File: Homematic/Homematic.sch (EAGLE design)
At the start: 26 parts, among them IC1 3.3V, IC2 3.3V, P1 DF11-06-2DS, Q1 BS170

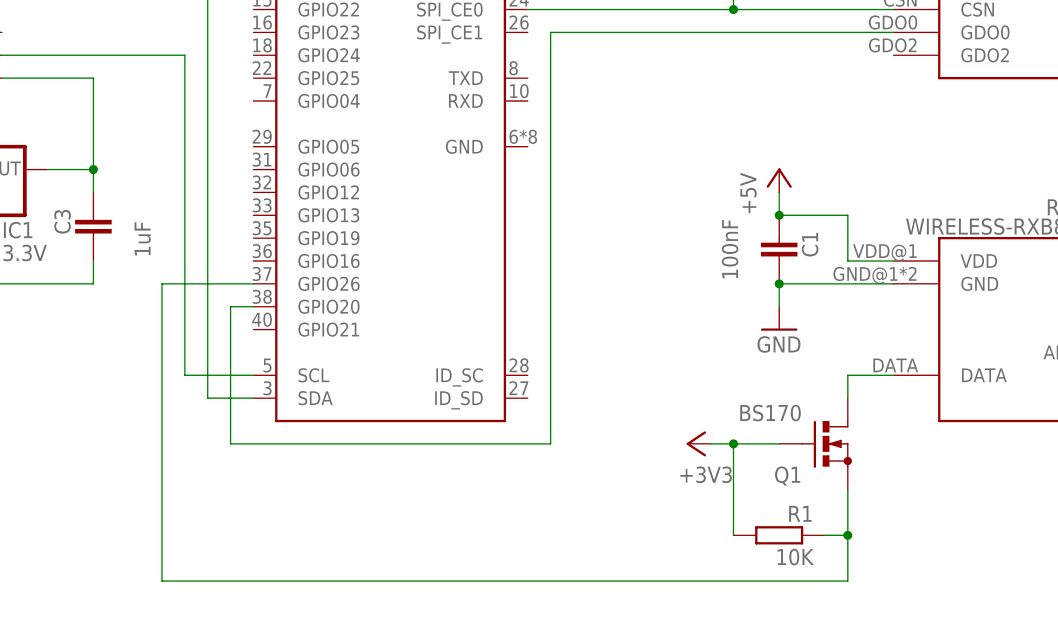
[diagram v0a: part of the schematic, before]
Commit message: Fix RXB8 package. Add low pass filter.
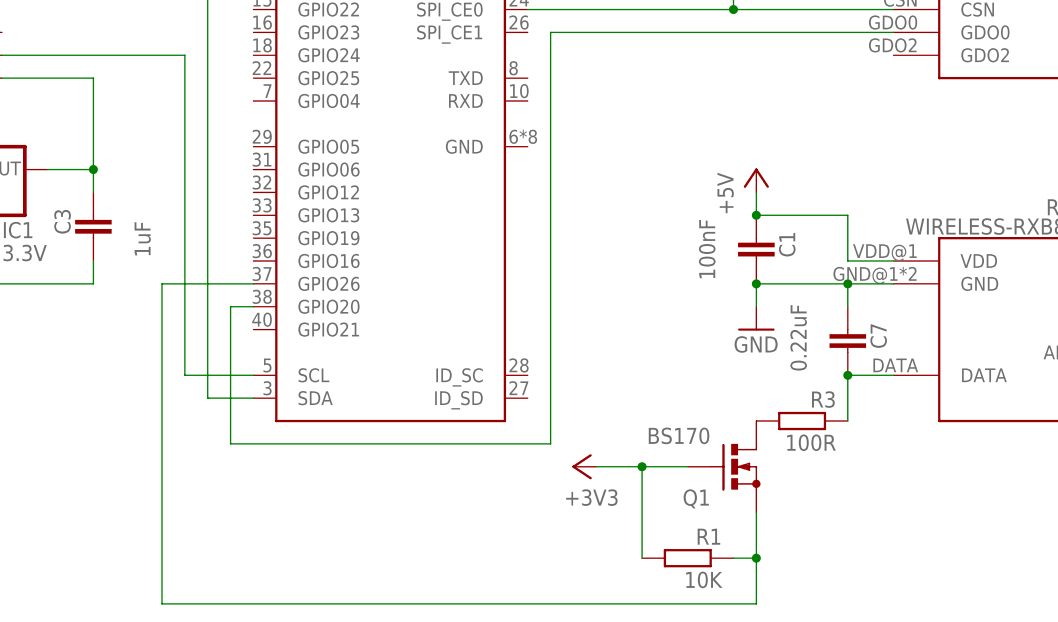
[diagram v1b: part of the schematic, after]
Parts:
- added C7: 0.22uF, capacitor-wima:C2,5-3
- added R3: 100R, rcl:R-EU_0204/5
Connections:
- new net N$11: Q1.D, R3.2
- net GND: now also C7.1
- net N$3: now also C7.2, R3.1; no longer Q1.D
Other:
- moved on the sheet: C1, Q1, R1
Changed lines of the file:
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@@
 <part name="+3V1" library="supply1" deviceset="+3V3" device=""/>
 <part name="+3V2" library="supply1" deviceset="+3V3" device=""/>
+<part name="R3" library="rcl" deviceset="R-EU_" device="0204/5" value="100R">
+<attribute name="MF" value=""/>
+<attribute name="MPN" value=""/>
+<attribute name="OC_FARNELL" value="unknown"/>
+</part>
+<part name="C7" library="capacitor-wima" deviceset="C" device="2,5-3" value="0.22uF"/>
 </parts>
 <sheets>
@@
 </instance>
 <instance part="GND2" gate="1" x="256.54" y="27.94"/>
-<instance part="Q1" gate="1" x="208.28" y="27.94" smashed="yes">
-<attribute name="OC_FARNELL" x="208.28" y="27.94" size="1.778" layer="96" rot="R270" display="off"/>
-<attribute name="MF" x="208.28" y="27.94" size="1.778" layer="96" rot="R270" display="off"/>
-<attribute name="MPN" x="208.28" y="27.94" size="1.778" layer="96" rot="R270" display="off"/>
-<attribute name="NAME" x="205.74" y="25.4" size="1.778" layer="95" align="top-right"/>
-<attribute name="VALUE" x="205.74" y="30.48" size="1.778" layer="96" align="bottom-right"/>
-</instance>
-<instance part="R1" gate="G$1" x="203.2" y="17.78" rot="MR0">
-<attribute name="OC_FARNELL" x="203.2" y="17.78" size="1.778" layer="96" rot="MR270" display="off"/>
-<attribute name="MF" x="203.2" y="17.78" size="1.778" layer="96" rot="MR270" display="off"/>
-<attribute name="MPN" x="203.2" y="17.78" size="1.778" layer="96" rot="MR270" display="off"/>
+<instance part="Q1" gate="1" x="198.12" y="25.4" smashed="yes">
+<attribute name="OC_FARNELL" x="198.12" y="25.4" size="1.778" layer="96" rot="R270" display="off"/>
+<attribute name="MF" x="198.12" y="25.4" size="1.778" layer="96" rot="R270" display="off"/>
+<attribute name="MPN" x="198.12" y="25.4" size="1.778" layer="96" rot="R270" display="off"/>
+<attribute name="NAME" x="195.58" y="22.86" size="1.778" layer="95" align="top-right"/>
+<attribute name="VALUE" x="195.58" y="27.94" size="1.778" layer="96" align="bottom-right"/>
+</instance>
+<instance part="R1" gate="G$1" x="193.04" y="15.24" rot="MR0">
+<attribute name="OC_FARNELL" x="193.04" y="15.24" size="1.778" layer="96" rot="MR270" display="off"/>
+<attribute name="MF" x="193.04" y="15.24" size="1.778" layer="96" rot="MR270" display="off"/>
+<attribute name="MPN" x="193.04" y="15.24" size="1.778" layer="96" rot="MR270" display="off"/>
 </instance>
 <instance part="MP1584-2" gate="G$1" x="50.8" y="93.98"/>
@@
 <attribute name="MPN" x="198.12" y="91.44" size="1.778" layer="96" rot="MR0" display="off"/>
 </instance>
-<instance part="GND6" gate="1" x="203.2" y="40.64"/>
-<instance part="C1" gate="G$1" x="203.2" y="50.8" smashed="yes" rot="MR0">
-<attribute name="NAME" x="205.74" y="48.641" size="1.778" layer="95" rot="MR90"/>
-<attribute name="VALUE" x="196.85" y="46.101" size="1.778" layer="96" rot="MR90"/>
-</instance>
-<instance part="P+4" gate="1" x="203.2" y="58.42"/>
+<instance part="GND6" gate="1" x="200.66" y="40.64"/>
+<instance part="C1" gate="G$1" x="200.66" y="50.8" smashed="yes" rot="MR0">
+<attribute name="NAME" x="203.2" y="48.641" size="1.778" layer="95" rot="MR90"/>
+<attribute name="VALUE" x="194.31" y="46.101" size="1.778" layer="96" rot="MR90"/>
+</instance>
+<instance part="P+4" gate="1" x="200.66" y="58.42"/>
 <instance part="+3V1" gate="G$1" x="213.36" y="129.54"/>
-<instance part="+3V2" gate="G$1" x="193.04" y="27.94" rot="R90"/>
+<instance part="+3V2" gate="G$1" x="180.34" y="25.4" rot="R90"/>
+<instance part="R3" gate="G$1" x="205.74" y="30.48" rot="MR0">
+<attribute name="OC_FARNELL" x="205.74" y="30.48" size="1.778" layer="96" rot="MR270" display="off"/>
+<attribute name="MF" x="205.74" y="30.48" size="1.778" layer="96" rot="MR270" display="off"/>
+<attribute name="MPN" x="205.74" y="30.48" size="1.778" layer="96" rot="MR270" display="off"/>
+</instance>
+<instance part="C7" gate="G$1" x="210.82" y="40.64" smashed="yes" rot="MR0">
+<attribute name="NAME" x="213.36" y="38.481" size="1.778" layer="95" rot="MR90"/>
+<attribute name="VALUE" x="204.47" y="35.941" size="1.778" layer="96" rot="MR90"/>
+</instance>
 </instances>
 <busses>
@@
 <pinref part="RXB8" gate="G$1" pin="GND"/>
 <pinref part="GND6" gate="1" pin="GND"/>
-<wire x1="215.9" y1="45.72" x2="203.2" y2="45.72" width="0.1524" layer="91"/>
-<wire x1="203.2" y1="45.72" x2="203.2" y2="43.18" width="0.1524" layer="91"/>
+<wire x1="215.9" y1="45.72" x2="210.82" y2="45.72" width="0.1524" layer="91"/>
+<wire x1="210.82" y1="45.72" x2="200.66" y2="45.72" width="0.1524" layer="91"/>
+<wire x1="200.66" y1="45.72" x2="200.66" y2="43.18" width="0.1524" layer="91"/>
 <pinref part="C1" gate="G$1" pin="2"/>
-<junction x="203.2" y="45.72"/>
-</segment>
-</net>
-<net name="N$69" class="0">
-<segment>
-<pinref part="Q1" gate="1" pin="S"/>
-<wire x1="210.82" y1="22.86" x2="210.82" y2="17.78" width="0.1524" layer="91"/>
-<wire x1="208.28" y1="17.78" x2="210.82" y2="17.78" width="0.1524" layer="91"/>
-<wire x1="210.82" y1="17.78" x2="210.82" y2="12.7" width="0.1524" layer="91"/>
-<wire x1="210.82" y1="12.7" x2="134.62" y2="12.7" width="0.1524" layer="91"/>
-<wire x1="134.62" y1="12.7" x2="134.62" y2="45.72" width="0.1524" layer="91"/>
-<pinref part="R1" gate="G$1" pin="1"/>
-<junction x="210.82" y="17.78"/>
-<pinref part="RPI" gate="G$1" pin="GPIO26"/>
-<wire x1="134.62" y1="45.72" x2="144.78" y2="45.72" width="0.1524" layer="91"/>
+<junction x="200.66" y="45.72"/>
+<pinref part="C7" gate="G$1" pin="1"/>
+<wire x1="210.82" y1="43.18" x2="210.82" y2="45.72" width="0.1524" layer="91"/>
+<junction x="210.82" y="45.72"/>
 </segment>
 </net>
 <net name="N$3" class="0">
 <segment>
-<pinref part="Q1" gate="1" pin="D"/>
-<wire x1="210.82" y1="35.56" x2="210.82" y2="33.02" width="0.1524" layer="91"/>
 <wire x1="210.82" y1="35.56" x2="215.9" y2="35.56" width="0.1524" layer="91"/>
 <pinref part="RXB8" gate="G$1" pin="DATA"/>
+<pinref part="C7" gate="G$1" pin="2"/>
+<pinref part="R3" gate="G$1" pin="1"/>
+<wire x1="210.82" y1="35.56" x2="210.82" y2="30.48" width="0.1524" layer="91"/>
+<junction x="210.82" y="35.56"/>
 </segment>
 </net>
@@
 <segment>
 <pinref part="C1" gate="G$1" pin="1"/>
-<wire x1="203.2" y1="55.88" x2="203.2" y2="53.34" width="0.1524" layer="91"/>
-<wire x1="203.2" y1="53.34" x2="210.82" y2="53.34" width="0.1524" layer="91"/>
+<wire x1="200.66" y1="55.88" x2="200.66" y2="53.34" width="0.1524" layer="91"/>
+<wire x1="200.66" y1="53.34" x2="210.82" y2="53.34" width="0.1524" layer="91"/>
 <wire x1="210.82" y1="53.34" x2="210.82" y2="48.26" width="0.1524" layer="91"/>
 <pinref part="RXB8" gate="G$1" pin="VDD"/>
 <wire x1="210.82" y1="48.26" x2="215.9" y2="48.26" width="0.1524" layer="91"/>
 <pinref part="P+4" gate="1" pin="+5V"/>
-<junction x="203.2" y="53.34"/>
+<junction x="200.66" y="53.34"/>
 </segment>
 </net>
@@
 <pinref part="R1" gate="G$1" pin="2"/>
 <pinref part="Q1" gate="1" pin="G"/>
-<wire x1="203.2" y1="27.94" x2="198.12" y2="27.94" width="0.1524" layer="91"/>
-<wire x1="198.12" y1="27.94" x2="198.12" y2="17.78" width="0.1524" layer="91"/>
+<wire x1="193.04" y1="25.4" x2="187.96" y2="25.4" width="0.1524" layer="91"/>
+<wire x1="187.96" y1="25.4" x2="187.96" y2="15.24" width="0.1524" layer="91"/>
 <pinref part="+3V2" gate="G$1" pin="+3V3"/>
-<wire x1="198.12" y1="27.94" x2="195.58" y2="27.94" width="0.1524" layer="91"/>
-<junction x="198.12" y="27.94"/>
+<wire x1="187.96" y1="25.4" x2="182.88" y2="25.4" width="0.1524" layer="91"/>
+<junction x="187.96" y="25.4"/>
 </segment>
 </net>
@@
 </segment>
 </net>
+<net name="N$11" class="0">
+<segment>
+<pinref part="Q1" gate="1" pin="D"/>
+<pinref part="R3" gate="G$1" pin="2"/>
+</segment>
+</net>
+<net name="N$10" class="0">
+<segment>
+<wire x1="134.62" y1="10.16" x2="134.62" y2="45.72" width="0.1524" layer="91"/>
+<pinref part="RPI" gate="G$1" pin="GPIO26"/>
+<wire x1="134.62" y1="45.72" x2="144.78" y2="45.72" width="0.1524" layer="91"/>
+<pinref part="Q1" gate="1" pin="S"/>
+<wire x1="200.66" y1="20.32" x2="200.66" y2="15.24" width="0.1524" layer="91"/>
+<pinref part="R1" gate="G$1" pin="1"/>
+<wire x1="198.12" y1="15.24" x2="200.66" y2="15.24" width="0.1524" layer="91"/>
+<junction x="200.66" y="15.24"/>
+<wire x1="200.66" y1="15.24" x2="200.66" y2="10.16" width="0.1524" layer="91"/>
+<wire x1="134.62" y1="10.16" x2="200.66" y2="10.16" width="0.1524" layer="91"/>
+</segment>
+</net>

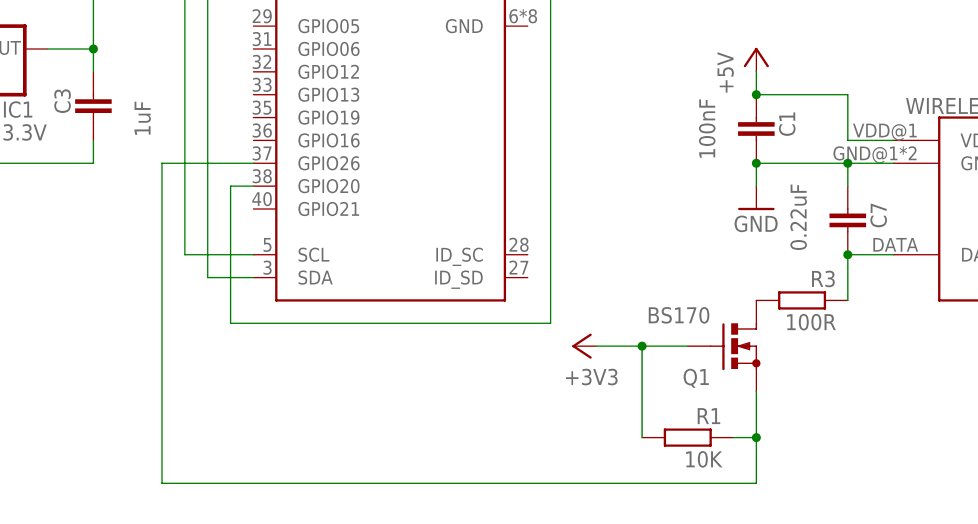
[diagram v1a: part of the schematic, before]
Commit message: Change low pass capacitor value from 220nF to 100nF.
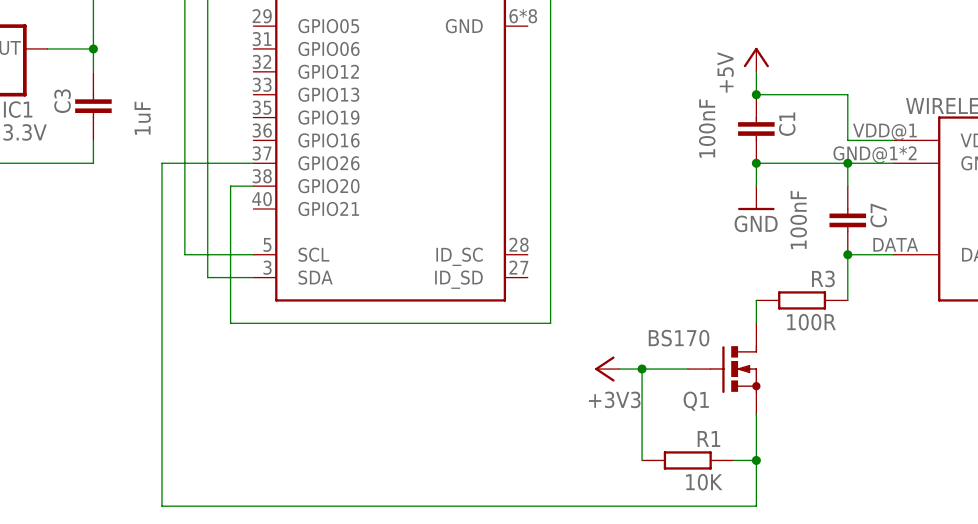
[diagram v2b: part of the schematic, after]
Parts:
- C7: value 0.22uF -> 100nF
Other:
- moved on the sheet: Q1, R1
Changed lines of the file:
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@@
 <attribute name="OC_FARNELL" value="unknown"/>
 </part>
-<part name="C7" library="capacitor-wima" deviceset="C" device="2,5-3" value="0.22uF"/>
+<part name="C7" library="capacitor-wima" deviceset="C" device="2,5-3" value="100nF"/>
 </parts>
 <sheets>
@@
 </instance>
 <instance part="GND2" gate="1" x="256.54" y="27.94"/>
-<instance part="Q1" gate="1" x="198.12" y="25.4" smashed="yes">
-<attribute name="OC_FARNELL" x="198.12" y="25.4" size="1.778" layer="96" rot="R270" display="off"/>
-<attribute name="MF" x="198.12" y="25.4" size="1.778" layer="96" rot="R270" display="off"/>
-<attribute name="MPN" x="198.12" y="25.4" size="1.778" layer="96" rot="R270" display="off"/>
-<attribute name="NAME" x="195.58" y="22.86" size="1.778" layer="95" align="top-right"/>
-<attribute name="VALUE" x="195.58" y="27.94" size="1.778" layer="96" align="bottom-right"/>
-</instance>
-<instance part="R1" gate="G$1" x="193.04" y="15.24" rot="MR0">
-<attribute name="OC_FARNELL" x="193.04" y="15.24" size="1.778" layer="96" rot="MR270" display="off"/>
-<attribute name="MF" x="193.04" y="15.24" size="1.778" layer="96" rot="MR270" display="off"/>
-<attribute name="MPN" x="193.04" y="15.24" size="1.778" layer="96" rot="MR270" display="off"/>
+<instance part="Q1" gate="1" x="198.12" y="22.86" smashed="yes">
+<attribute name="OC_FARNELL" x="198.12" y="22.86" size="1.778" layer="96" rot="R270" display="off"/>
+<attribute name="MF" x="198.12" y="22.86" size="1.778" layer="96" rot="R270" display="off"/>
+<attribute name="MPN" x="198.12" y="22.86" size="1.778" layer="96" rot="R270" display="off"/>
+<attribute name="NAME" x="195.58" y="20.32" size="1.778" layer="95" align="top-right"/>
+<attribute name="VALUE" x="195.58" y="25.4" size="1.778" layer="96" align="bottom-right"/>
+</instance>
+<instance part="R1" gate="G$1" x="193.04" y="12.7" rot="MR0">
+<attribute name="OC_FARNELL" x="193.04" y="12.7" size="1.778" layer="96" rot="MR270" display="off"/>
+<attribute name="MF" x="193.04" y="12.7" size="1.778" layer="96" rot="MR270" display="off"/>
+<attribute name="MPN" x="193.04" y="12.7" size="1.778" layer="96" rot="MR270" display="off"/>
 </instance>
 <instance part="MP1584-2" gate="G$1" x="50.8" y="93.98"/>
@@
 <instance part="P+4" gate="1" x="200.66" y="58.42"/>
 <instance part="+3V1" gate="G$1" x="213.36" y="129.54"/>
-<instance part="+3V2" gate="G$1" x="180.34" y="25.4" rot="R90"/>
+<instance part="+3V2" gate="G$1" x="182.88" y="22.86" rot="R90"/>
 <instance part="R3" gate="G$1" x="205.74" y="30.48" rot="MR0">
 <attribute name="OC_FARNELL" x="205.74" y="30.48" size="1.778" layer="96" rot="MR270" display="off"/>
@@
 <pinref part="R1" gate="G$1" pin="2"/>
 <pinref part="Q1" gate="1" pin="G"/>
-<wire x1="193.04" y1="25.4" x2="187.96" y2="25.4" width="0.1524" layer="91"/>
-<wire x1="187.96" y1="25.4" x2="187.96" y2="15.24" width="0.1524" layer="91"/>
+<wire x1="193.04" y1="22.86" x2="187.96" y2="22.86" width="0.1524" layer="91"/>
+<wire x1="187.96" y1="22.86" x2="187.96" y2="12.7" width="0.1524" layer="91"/>
 <pinref part="+3V2" gate="G$1" pin="+3V3"/>
-<wire x1="187.96" y1="25.4" x2="182.88" y2="25.4" width="0.1524" layer="91"/>
-<junction x="187.96" y="25.4"/>
+<wire x1="187.96" y1="22.86" x2="185.42" y2="22.86" width="0.1524" layer="91"/>
+<junction x="187.96" y="22.86"/>
 </segment>
 </net>
@@
 <pinref part="Q1" gate="1" pin="D"/>
 <pinref part="R3" gate="G$1" pin="2"/>
+<wire x1="200.66" y1="27.94" x2="200.66" y2="30.48" width="0.1524" layer="91"/>
 </segment>
 </net>
 <net name="N$10" class="0">
 <segment>
-<wire x1="134.62" y1="10.16" x2="134.62" y2="45.72" width="0.1524" layer="91"/>
+<wire x1="134.62" y1="7.62" x2="134.62" y2="45.72" width="0.1524" layer="91"/>
 <pinref part="RPI" gate="G$1" pin="GPIO26"/>
 <wire x1="134.62" y1="45.72" x2="144.78" y2="45.72" width="0.1524" layer="91"/>
 <pinref part="Q1" gate="1" pin="S"/>
-<wire x1="200.66" y1="20.32" x2="200.66" y2="15.24" width="0.1524" layer="91"/>
+<wire x1="200.66" y1="17.78" x2="200.66" y2="12.7" width="0.1524" layer="91"/>
 <pinref part="R1" gate="G$1" pin="1"/>
-<wire x1="198.12" y1="15.24" x2="200.66" y2="15.24" width="0.1524" layer="91"/>
-<junction x="200.66" y="15.24"/>
-<wire x1="200.66" y1="15.24" x2="200.66" y2="10.16" width="0.1524" layer="91"/>
-<wire x1="134.62" y1="10.16" x2="200.66" y2="10.16" width="0.1524" layer="91"/>
-</segment>
-</net>
+<wire x1="198.12" y1="12.7" x2="200.66" y2="12.7" width="0.1524" layer="91"/>
+<junction x="200.66" y="12.7"/>
+<wire x1="200.66" y1="12.7" x2="200.66" y2="7.62" width="0.1524" layer="91"/>
+<wire x1="134.62" y1="7.62" x2="200.66" y2="7.62" width="0.1524" layer="91"/>
+</segment>
+</net>
